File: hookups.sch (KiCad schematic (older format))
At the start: 16 parts, among them P12 CONN_01X02, P24 CONN_01X02, P25 CONN_01X02, P26 CONN_01X02, P27 CONN_01X02, P28 CONN_01X02, P29 CONN_02X02, P30 CONN_02X02, P31 CONN_01X02, P32 CONN_01X02, P33 CONN_01X02, P34 CONN_01X02, P35 CONN_02X02, P36 CONN_01X02, P37 CONN_02X02, P38 CONN_01X02

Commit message: reordered all reference designators
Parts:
- renumbered P12 to P19, P24 to P20, P25 to P21, P26 to P22, P27 to P23, P28 to P24, P29 to P25, P30 to P26, P31 to P27, P32 to P28, P33 to P29, P34 to P30, P35 to P31, P36 to P32, P37 to P33, P38 to P34
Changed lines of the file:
@@
 $EndDescr
 $Comp
-L CONN_01X02 P12
+L CONN_01X02 P19
 U 1 1 573832BB
 P 1950 850
-F 0 "P12" H 1950 1000 50  0000 C CNN
+F 0 "P19" H 1950 1000 50  0000 C CNN
 F 1 "CONN_01X02" V 2050 850 50  0001 C CNN
 F 2 "Pin_Headers:Pin_Header_Straight_1x02" H 1950 850 50  0001 C CNN
@@
 RLY-IHV-HIGH
 $Comp
-L CONN_01X02 P24
+L CONN_01X02 P20
 U 1 1 5738574C
 P 1950 1250
-F 0 "P24" H 1950 1400 50  0000 C CNN
+F 0 "P20" H 1950 1400 50  0000 C CNN
 F 1 "CONN_01X02" V 2050 1250 50  0001 C CNN
 F 2 "Pin_Headers:Pin_Header_Straight_1x02" H 1950 1250 50  0001 C CNN
@@
 RLY-IHV-LOW
 $Comp
-L CONN_01X02 P25
+L CONN_01X02 P21
 U 1 1 5738577B
 P 1950 1650
-F 0 "P25" H 1950 1800 50  0000 C CNN
+F 0 "P21" H 1950 1800 50  0000 C CNN
 F 1 "CONN_01X02" V 2050 1650 50  0001 C CNN
 F 2 "Pin_Headers:Pin_Header_Straight_1x02" H 1950 1650 50  0001 C CNN
@@
 RLY-ILV
 $Comp
-L CONN_01X02 P26
+L CONN_01X02 P22
 U 1 1 573858EE
 P 1950 2050
-F 0 "P26" H 1950 2200 50  0000 C CNN
+F 0 "P22" H 1950 2200 50  0000 C CNN
 F 1 "CONN_01X02" V 2050 2050 50  0001 C CNN
 F 2 "Pin_Headers:Pin_Header_Straight_1x02" H 1950 2050 50  0001 C CNN
@@
 RLY-DCDC
 $Comp
-L CONN_01X02 P27
+L CONN_01X02 P23
 U 1 1 57385969
 P 1950 2450
-F 0 "P27" H 1950 2600 50  0000 C CNN
+F 0 "P23" H 1950 2600 50  0000 C CNN
 F 1 "CONN_01X02" V 2050 2450 50  0001 C CNN
 F 2 "Pin_Headers:Pin_Header_Straight_1x02" H 1950 2450 50  0001 C CNN
@@
 +5V
 $Comp
-L CONN_01X02 P28
+L CONN_01X02 P24
 U 1 1 573859A3
 P 1950 2850
-F 0 "P28" H 1950 3000 50  0000 C CNN
+F 0 "P24" H 1950 3000 50  0000 C CNN
 F 1 "CONN_01X02" V 2050 2850 50  0001 C CNN
 F 2 "Pin_Headers:Pin_Header_Straight_1x02" H 1950 2850 50  0001 C CNN
@@
 HV-CURR
 $Comp
-L CONN_01X02 P31
+L CONN_01X02 P27
 U 1 1 57386EC1
 P 1950 4050
-F 0 "P31" H 1950 4200 50  0000 C CNN
+F 0 "P27" H 1950 4200 50  0000 C CNN
 F 1 "CONN_01X02" V 2050 4050 50  0001 C CNN
 F 2 "Pin_Headers:Pin_Header_Straight_1x02" H 1950 4050 50  0001 C CNN
@@
 IHV-PRECHG
 $Comp
-L CONN_01X02 P32
+L CONN_01X02 P28
 U 1 1 57386ECC
 P 1950 4450
-F 0 "P32" H 1950 4600 50  0000 C CNN
+F 0 "P28" H 1950 4600 50  0000 C CNN
 F 1 "CONN_01X02" V 2050 4450 50  0001 C CNN
 F 2 "Pin_Headers:Pin_Header_Straight_1x02" H 1950 4450 50  0001 C CNN
@@
 ILV-PRECHG
 $Comp
-L CONN_01X02 P33
+L CONN_01X02 P29
 U 1 1 5738711D
 P 1950 4850
-F 0 "P33" H 1950 5000 50  0000 C CNN
+F 0 "P29" H 1950 5000 50  0000 C CNN
 F 1 "CONN_01X02" V 2050 4850 50  0001 C CNN
 F 2 "Pin_Headers:Pin_Header_Straight_1x02" H 1950 4850 50  0001 C CNN
@@
 SENS-SDA
 $Comp
-L CONN_01X02 P34
+L CONN_01X02 P30
 U 1 1 57387128
 P 1950 5250
-F 0 "P34" H 1950 5400 50  0000 C CNN
+F 0 "P30" H 1950 5400 50  0000 C CNN
 F 1 "CONN_01X02" V 2050 5250 50  0001 C CNN
 F 2 "Pin_Headers:Pin_Header_Straight_1x02" H 1950 5250 50  0001 C CNN
@@
 SENS-SCL
 $Comp
-L CONN_02X02 P35
+L CONN_02X02 P31
 U 1 1 5738733F
 P 1900 5650
-F 0 "P35" H 1900 5800 50  0000 C CNN
+F 0 "P31" H 1900 5800 50  0000 C CNN
 F 1 "CONN_02X02" H 1900 5500 50  0001 C CNN
 F 2 "Pin_Headers:Pin_Header_Straight_2x02" H 1900 4450 50  0001 C CNN
@@
 +24V
 $Comp
-L CONN_01X02 P36
+L CONN_01X02 P32
 U 1 1 57387803
 P 1950 6200
-F 0 "P36" H 1950 6350 50  0000 C CNN
+F 0 "P32" H 1950 6350 50  0000 C CNN
 F 1 "CONN_01X02" V 2050 6200 50  0001 C CNN
 F 2 "Pin_Headers:Pin_Header_Straight_1x02" H 1950 6200 50  0001 C CNN
@@
 +3.3V
 $Comp
-L CONN_02X02 P29
+L CONN_02X02 P25
 U 1 1 5738CCEF
 P 1950 3250
-F 0 "P29" H 1950 3400 50  0000 C CNN
+F 0 "P25" H 1950 3400 50  0000 C CNN
 F 1 "CONN_02X02" H 1950 3100 50  0001 C CNN
 F 2 "Pin_Headers:Pin_Header_Straight_2x02" H 1950 2050 50  0001 C CNN
@@
 GLV
 $Comp
-L CONN_02X02 P30
+L CONN_02X02 P26
 U 1 1 5738D490
 P 1950 3650
-F 0 "P30" H 1950 3800 50  0000 C CNN
+F 0 "P26" H 1950 3800 50  0000 C CNN
 F 1 "CONN_02X02" H 1950 3500 50  0001 C CNN
 F 2 "Pin_Headers:Pin_Header_Straight_2x02" H 1950 2450 50  0001 C CNN
@@
 Connection ~ 2300 3600
 $Comp
-L CONN_02X02 P37
+L CONN_02X02 P33
 U 1 1 5738DEBF
 P 1950 6600
-F 0 "P37" H 1950 6750 50  0000 C CNN
+F 0 "P33" H 1950 6750 50  0000 C CNN
 F 1 "CONN_02X02" H 1950 6450 50  0001 C CNN
 F 2 "Pin_Headers:Pin_Header_Straight_2x02" H 1950 5400 50  0001 C CNN
@@
 +24V
 $Comp
-L CONN_01X02 P38
+L CONN_01X02 P34
 U 1 1 5738EB27
 P 1950 7000
-F 0 "P38" H 1950 7150 50  0000 C CNN
+F 0 "P34" H 1950 7150 50  0000 C CNN
 F 1 "CONN_01X02" V 2050 7000 50  0001 C CNN
 F 2 "Pin_Headers:Pin_Header_Straight_1x02" H 1950 7000 50  0001 C CNN

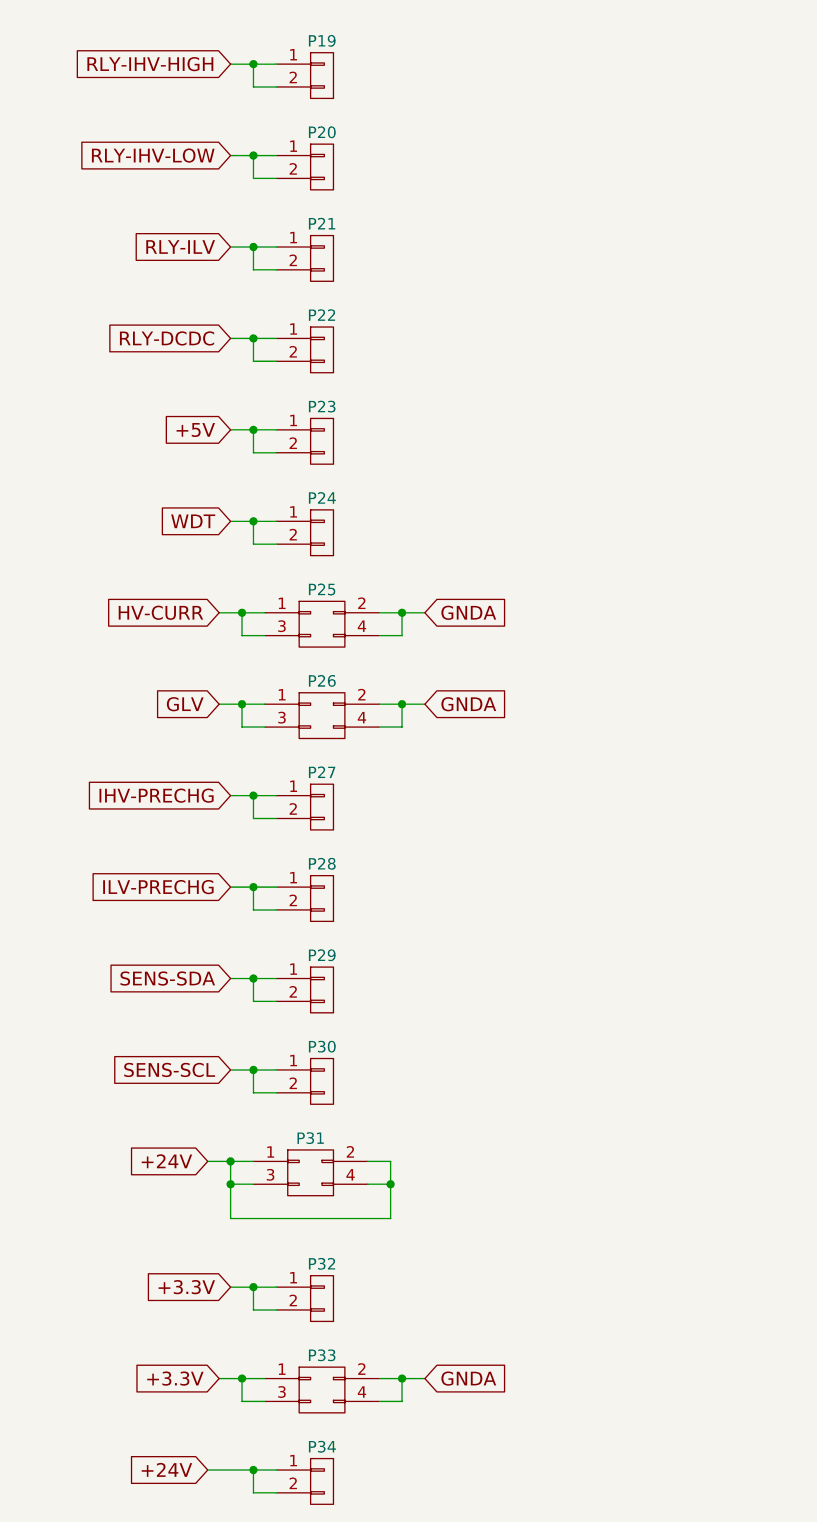
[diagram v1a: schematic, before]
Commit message: laid out BMS section
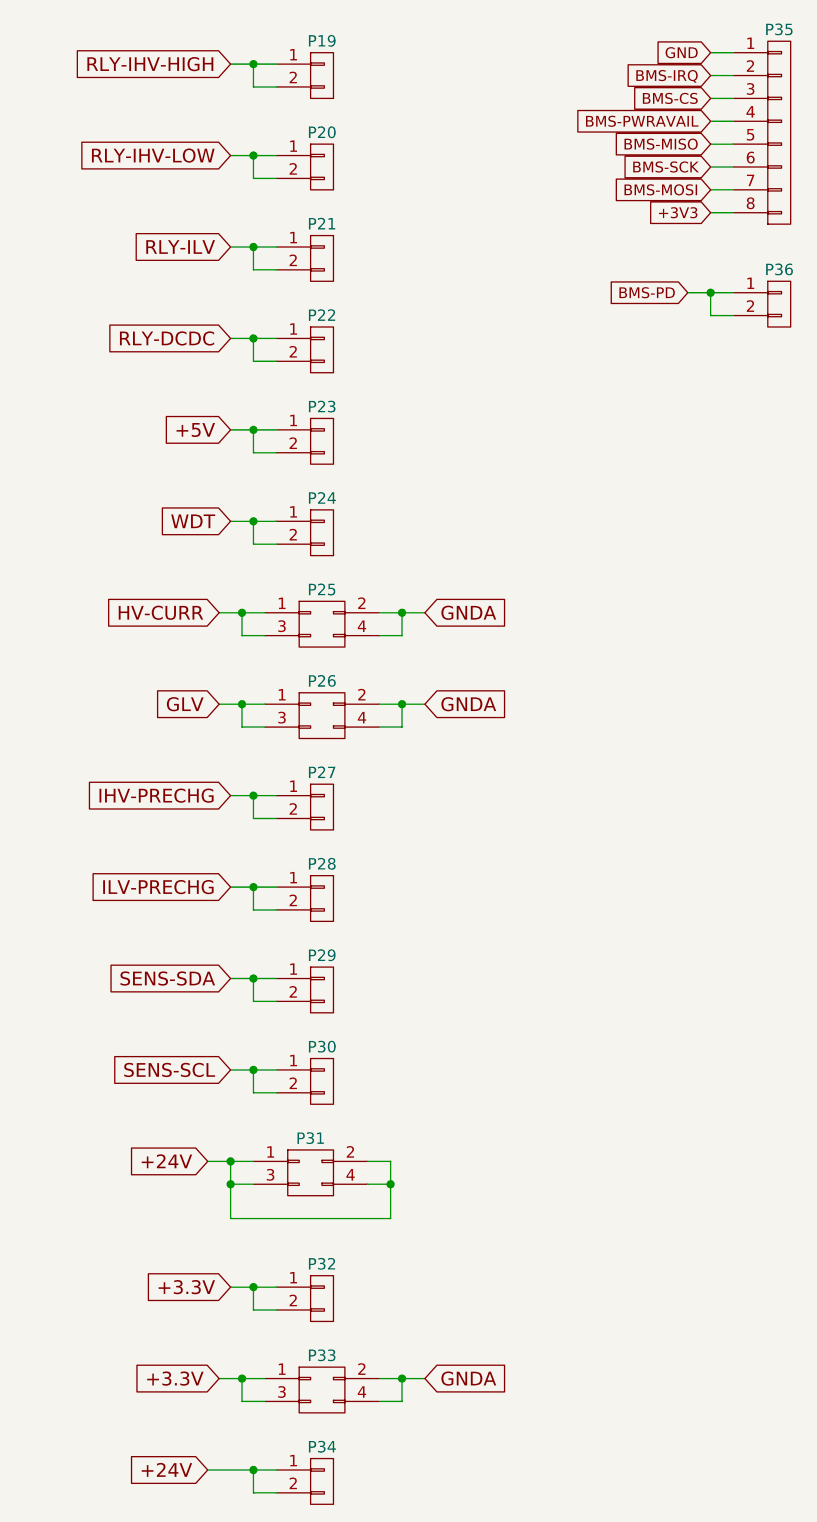
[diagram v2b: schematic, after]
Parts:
- added P35: CONN_01X08, Pin_Headers:Pin_Header_Straight_1x08, symbol CONN_01X08
- added P36: CONN_01X02, Pin_Headers:Pin_Header_Straight_1x02, symbol CONN_01X02
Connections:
- new net +3V3: P35.8 (P8)
- new net BMS-CS: P35.3 (P3)
- new net BMS-IRQ: P35.2 (P2)
- new net BMS-MISO: P35.5 (P5)
- new net BMS-MOSI: P35.7 (P7)
- new net BMS-PD: P36.1 (P1), P36.2 (P2)
- new net BMS-PWRAVAIL: P35.4 (P4)
- new net BMS-SCK: P35.6 (P6)
- new net GND: P35.1 (P1)
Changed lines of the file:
@@
 $EndComp
 Wire Wire Line
-	1750 800  1550 800
+	1550 800  1750 800
 Wire Wire Line
 	1750 900  1650 900
@@
 $EndComp
 Wire Wire Line
-	1750 1200 1550 1200
+	1550 1200 1750 1200
 Wire Wire Line
 	1750 1300 1650 1300
@@
 $EndComp
 Wire Wire Line
-	1750 1600 1550 1600
+	1550 1600 1750 1600
 Wire Wire Line
 	1750 1700 1650 1700
@@
 $EndComp
 Wire Wire Line
-	1750 2000 1550 2000
+	1550 2000 1750 2000
 Wire Wire Line
 	1750 2100 1650 2100
@@
 $EndComp
 Wire Wire Line
-	1750 2400 1550 2400
+	1550 2400 1750 2400
 Wire Wire Line
 	1750 2500 1650 2500
@@
 $EndComp
 Wire Wire Line
-	1750 2800 1550 2800
+	1550 2800 1750 2800
 Wire Wire Line
 	1750 2900 1650 2900
@@
 $EndComp
 Wire Wire Line
-	1750 4000 1550 4000
+	1550 4000 1750 4000
 Wire Wire Line
 	1750 4100 1650 4100
@@
 $EndComp
 Wire Wire Line
-	1750 4400 1550 4400
+	1550 4400 1750 4400
 Wire Wire Line
 	1750 4500 1650 4500
@@
 $EndComp
 Wire Wire Line
-	1750 4800 1550 4800
+	1550 4800 1750 4800
 Wire Wire Line
 	1750 4900 1650 4900
@@
 $EndComp
 Wire Wire Line
-	1750 5200 1550 5200
+	1550 5200 1750 5200
 Wire Wire Line
 	1750 5300 1650 5300
@@
 $EndComp
 Wire Wire Line
-	1650 5600 1450 5600
+	1450 5600 1650 5600
 Wire Wire Line
 	1650 5700 1550 5700
@@
 $EndComp
 Wire Wire Line
-	1750 6150 1550 6150
+	1550 6150 1750 6150
 Wire Wire Line
 	1750 6250 1650 6250
@@
 +3.3V
 Wire Wire Line
-	1700 6550 1500 6550
+	1500 6550 1700 6550
 Wire Wire Line
 	1700 6650 1600 6650
@@
 $EndComp
 Wire Wire Line
-	1750 6950 1450 6950
+	1450 6950 1750 6950
 Wire Wire Line
 	1750 7050 1650 7050
@@
 	1650 7050 1650 6950
 Connection ~ 1650 6950
+$Comp
+L CONN_01X08 P35
+U 1 1 575063C4
+P 3950 1100
+F 0 "P35" H 3950 1550 50  0000 C CNN
+F 1 "CONN_01X08" V 4050 1100 50  0001 C CNN
+F 2 "Pin_Headers:Pin_Header_Straight_1x08" H 3950 1100 50  0001 C CNN
+F 3 "" H 3950 1100 50  0000 C CNN
+	1    3950 1100
+	1    0    0    -1
+$EndComp
+Wire Wire Line
+	3750 750  3650 750
+Wire Wire Line
+	3750 850  3650 850
+Wire Wire Line
+	3750 950  3650 950
+Wire Wire Line
+	3750 1050 3650 1050
+Wire Wire Line
+	3750 1150 3650 1150
+Wire Wire Line
+	3750 1250 3650 1250
+Wire Wire Line
+	3750 1350 3650 1350
+Wire Wire Line
+	3750 1450 3650 1450
+Text GLabel 3650 750  0    47   Input ~ 0
+GND
+Text GLabel 3650 850  0    47   Input ~ 0
+BMS-IRQ
+Text GLabel 3650 950  0    47   Input ~ 0
+BMS-CS
+Text GLabel 3650 1050 0    47   Input ~ 0
+BMS-PWRAVAIL
+Text GLabel 3650 1150 0    47   Input ~ 0
+BMS-MISO
+Text GLabel 3650 1250 0    47   Input ~ 0
+BMS-SCK
+Text GLabel 3650 1350 0    47   Input ~ 0
+BMS-MOSI
+Text GLabel 3650 1450 0    47   Input ~ 0
++3V3
+$Comp
+L CONN_01X02 P36
+U 1 1 57507872
+P 3950 1850
+F 0 "P36" H 3950 2000 50  0000 C CNN
+F 1 "CONN_01X02" V 4050 1850 50  0001 C CNN
+F 2 "Pin_Headers:Pin_Header_Straight_1x02" H 3950 1850 50  0001 C CNN
+F 3 "" H 3950 1850 50  0000 C CNN
+	1    3950 1850
+	1    0    0    -1
+$EndComp
+Text GLabel 3550 1800 0    47   Input ~ 0
+BMS-PD
+Wire Wire Line
+	3550 1800 3750 1800
+Wire Wire Line
+	3750 1900 3650 1900
+Wire Wire Line
+	3650 1900 3650 1800
+Connection ~ 3650 1800
 $EndSCHEMATC
